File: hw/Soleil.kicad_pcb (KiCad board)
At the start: 2 copper layers, 31.4 x 44 mm, 51 parts, among them J1 Conn_01x04, Q1 MMBT3904, Q2 2N7002, SW1 SW_Push, U1 SPV1040TTR, U2 XS3A1T3157GMX, U3 TPS61220DCK, U4 STM32G030F6Px, U5 ZJY200200-0154DAAMFGN, U6 W25Q16JVUXIQ

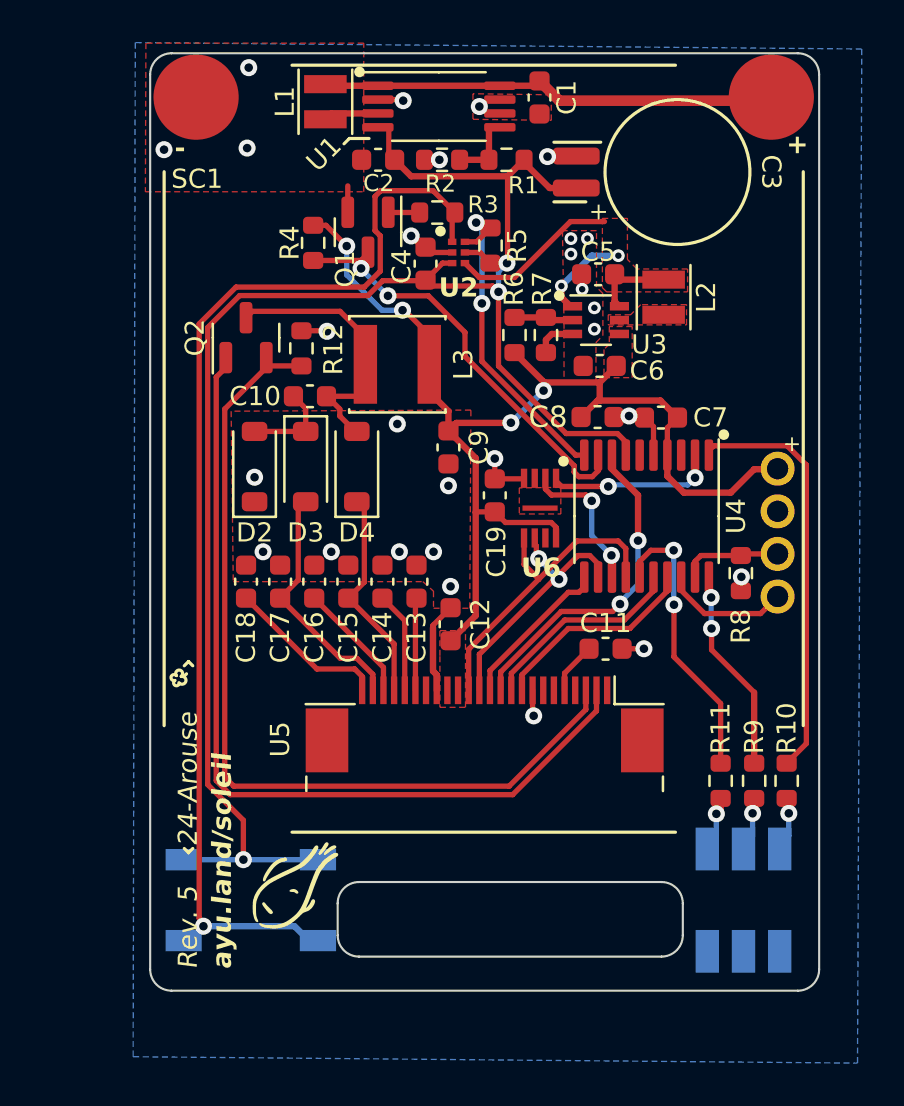
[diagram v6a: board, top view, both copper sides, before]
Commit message: Revise hardware; fix phantom powering
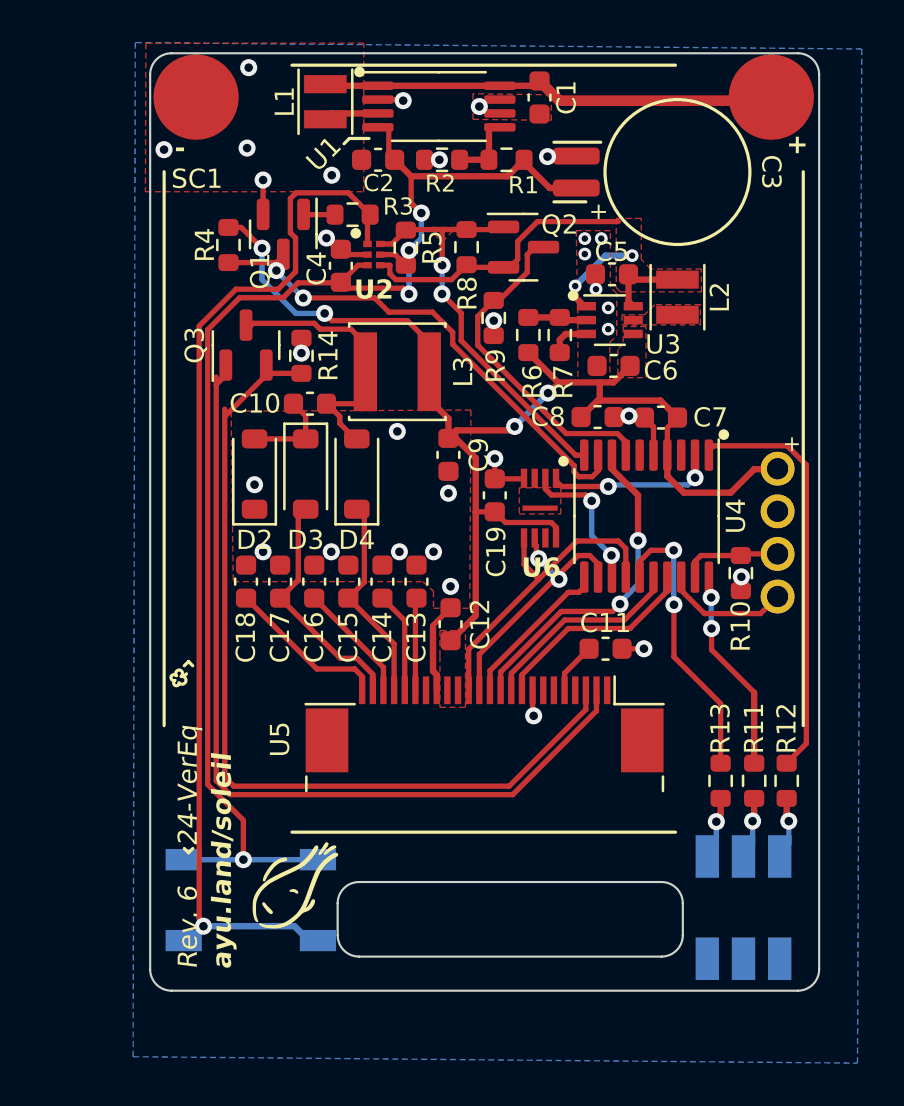
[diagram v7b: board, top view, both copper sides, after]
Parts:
- added Q2: Si2301, Package_TO_SOT_SMD:SOT-23, F.Cu at (23.6, 18.5)
- added R8: 1M, Resistor_SMD:R_0603_1608Metric, F.Cu at (20.9, 18.5)
- added R9: 1M, Resistor_SMD:R_0603_1608Metric, F.Cu at (22.2, 21.8)
- moved Q1 3.98 mm to (12.3, 17.9)
- moved R3 3.98 mm to (15.6, 17.0)
- moved R4 3.98 mm to (9.78, 18.4)
- moved C4 3.98 mm to (15.1, 19.4)
- moved R5 3.98 mm to (18.1, 18.5)
- moved U2 3.98 mm to (16.6, 18.9)
- moved C6 0.65 mm to (27.9, 24.1)
- moved L2 0.65 mm to (30.9, 20.9)
- moved R6 0.65 mm to (23.9, 22.6)
- moved U3 0.65 mm to (27.7, 21.9)
- moved C5 0.65 mm to (27.8, 19.8)
- moved R7 0.65 mm to (25.3, 22.6)
- moved C10 0.35 mm to (13.6, 25.9)
- moved C9 0.35 mm to (20.1, 28.2)
- moved D1 0.35 mm to (34.0, 49.5)
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- renumbered Q2 to Q3, R8 to R10, R9 to R11, R10 to R12, R11 to R13, R12 to R14
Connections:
- U4 pad 7: VCAP -> VRI_SENSE
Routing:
- net VRI_SENSE: track 0.00 -> 15.7 mm
- net VCAP: track 79.6 -> 64.1 mm, vias 3 -> 4
- net VRI: track 16.4 -> 21.9 mm
- net VDD: track 55.6 -> 60.4 mm
- net PWR_LATCH: track 15.5 -> 19.7 mm
- net Net-(U2-Y2): track 53.7 -> 49.6 mm
- net BTN_INTR: track 20.5 -> 24.1 mm
- net GND: track 21.4 -> 21.7 mm, vias 28 -> 31
- added copper zone on F.Cu, net PWR_LATCH
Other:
- board text added: "24-VerEq"
- board text added: "Rev. 6"
- board text removed: "24-Arouse"
- board text removed: "Rev. 5"

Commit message: 🚧 Further revise hardware
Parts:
- moved C9 0.20 mm to (20.2, 28.1)
- moved R9 0.15 mm to (22.2, 22.0)
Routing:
- net VRI_SENSE: track 15.7 -> 14.3 mm
